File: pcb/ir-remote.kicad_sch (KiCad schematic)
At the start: 104 parts, among them J1 Conn_01x02, J12 Conn_01x04, J2 Conn_01x02, J3 Pins_02x04_P2.54mm_SMT, J4 USB-C_Receptacle_Molex_217179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, J5 Jack_RCA_Stereo, J6 Conn_01x03, J7 Jack_RCA_Stereo, J8 Conn_01x02, U1 STM32G431CBTx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

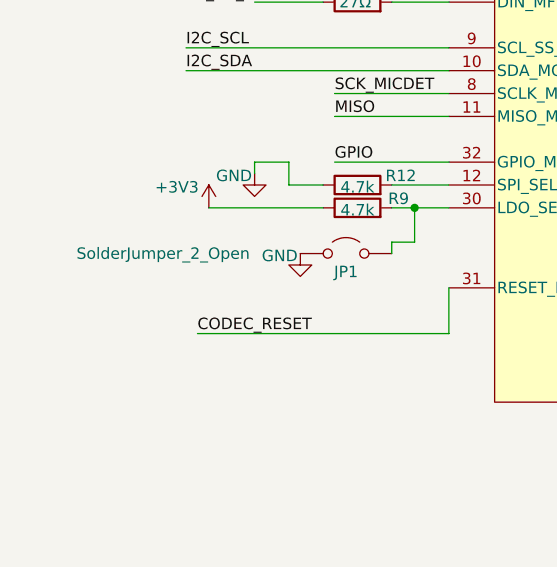
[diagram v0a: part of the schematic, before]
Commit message: Note on PCB about jumper
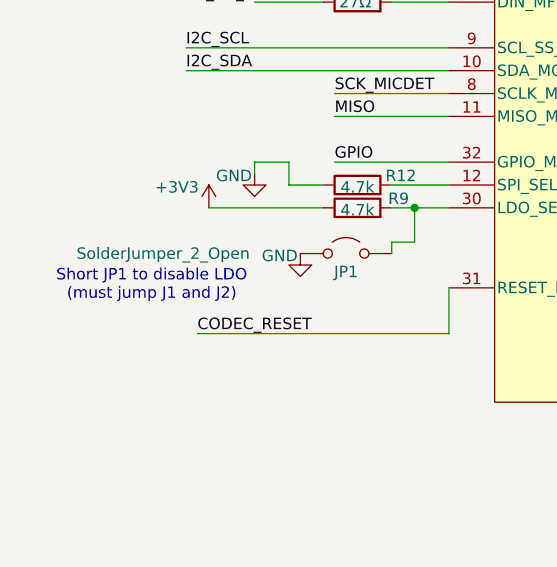
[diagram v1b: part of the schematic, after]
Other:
- note added: "Short JP1 to disable LDO (must jump J1 and J2)"
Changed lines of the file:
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@@
 		)
 	)
+	(text "Short JP1 to disable LDO\n(must jump J1 and J2)"
+		(exclude_from_sim no)
+		(at 27.94 268.986 0)
+		(effects
+			(font
+				(size 1.27 1.27)
+			)
+		)
+	)
 	(text "AUDIO"
 		(exclude_from_sim no)
@@
 		(at 320.04 443.23 0)
 		(unit 1)
-		(exclude_from_sim no)
+		(exclude_from_sim yes)
 		(in_bom no)
 		(on_board no)
@@
 			(at 320.04 443.23 0)
 			(effects
-				(font
-					(size 1.27 1.27)
-				)
-				(hide yes)
-			)
-		)
-		(property "Sim.Enable" "0"
-			(at 320.04 443.23 0)
-			(effects
